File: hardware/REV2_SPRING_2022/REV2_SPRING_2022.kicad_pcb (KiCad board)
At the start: 2 copper layers, 108 x 304.8 mm, 52 parts, among them J101 Screw_Terminal_01x02, J102 Screw_Terminal_01x02, J103 Conn_01x02_Female, J104 Screw_Terminal_01x02, J105 Conn_01x02_Female, J106 Conn_01x02_Female, J107 Screw_Terminal_01x02, J108 Screw_Terminal_01x02, J109 Conn_01x02_Female, J110 Conn_01x02_Female, Q101 Q_NMOS_GDS, Q102 Q_NMOS_GDS, U1 Teensy3.6_All_Pins, U2 PA16165_Breakout, U201 TPS2113ADRBR, U3 MPL3115A2_Breakout, U301 TPS2113ADRBR, U4 BNO055_Breakout, U5 RFM69HCW_Breakout

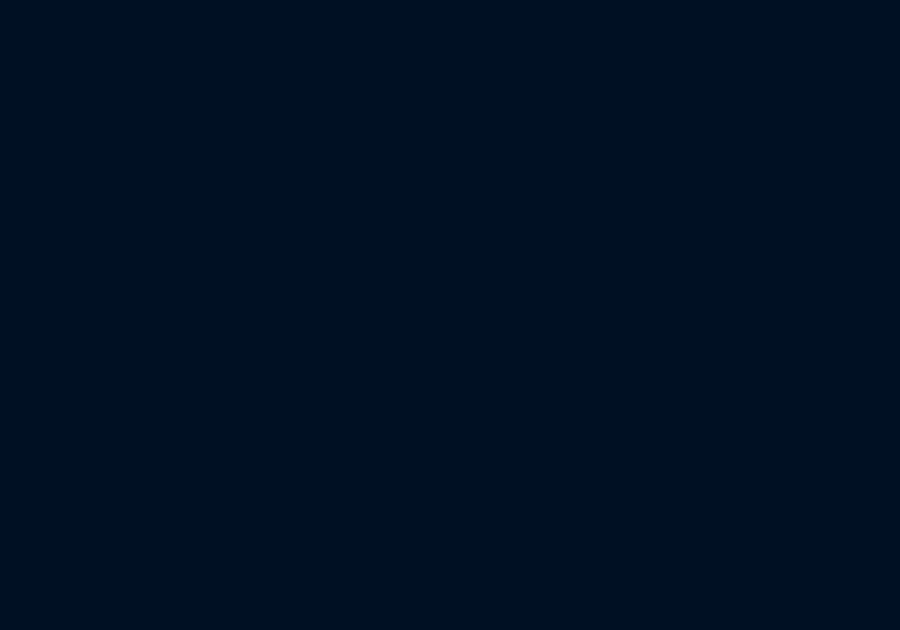
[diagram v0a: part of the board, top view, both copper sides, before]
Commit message: add another LED to schematic and layout
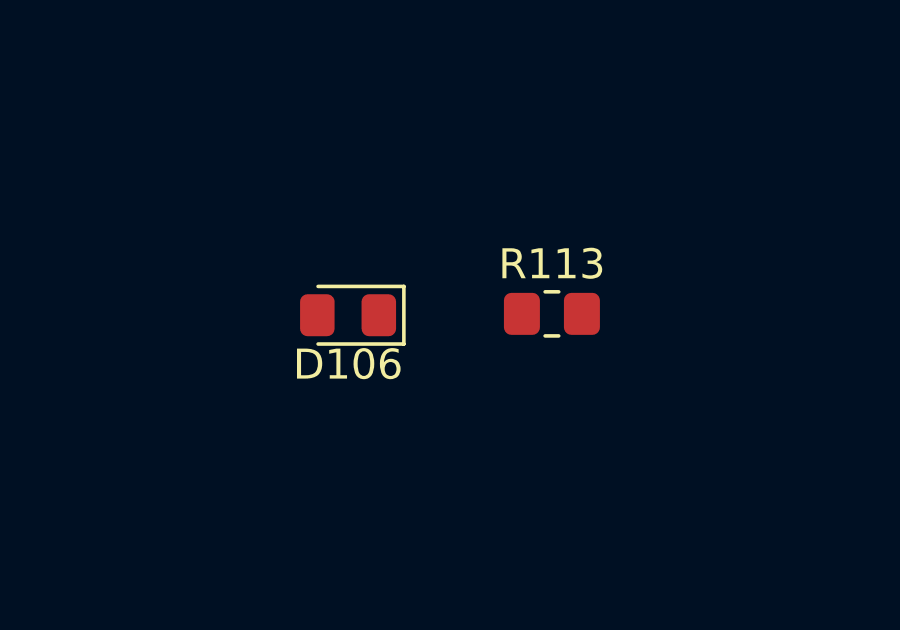
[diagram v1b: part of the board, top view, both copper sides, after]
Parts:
- added D106: LED, LED_SMD:LED_0805_2012Metric_Pad1.15x1.40mm_HandSolder, F.Cu at (197.9, 85.0)
- added R113: R_750, Resistor_SMD:R_0805_2012Metric_Pad1.20x1.40mm_HandSolder, F.Cu at (204.7, 85.0)
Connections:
- U1 pad 6: Net-(U1-Pad6) -> /BUZZER
- U1 pad 7: /BUZZER -> /LED_0

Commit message: wip
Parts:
- moved BZ101 398.2 mm to (-146.5, 21.5)
- moved R112 369.1 mm to (-97.5, -41.5), turned to 180 degrees
- moved J107 347.8 mm to (-82.8, -51.2), turned to 180 degrees
- moved R111 319.2 mm to (-46.8, -43.2), turned to 180 degrees
- moved J109 301.9 mm to (-67.8, -10.8), turned to 180 degrees
- moved J105 295.3 mm to (-82.5, -10.5), turned to 180 degrees
- moved R107 286.6 mm to (-125.5, 148.4), turned to 180 degrees
- moved R106 284.9 mm to (-125.5, 142.3), turned to 180 degrees
- moved R105 283.8 mm to (-125.5, 136.2), turned to 180 degrees
- moved R104 283.1 mm to (-125.5, 130.1), turned to 180 degrees
- moved R108 282.9 mm to (-122.4, 154.5), turned to 180 degrees
- moved J110 278.5 mm to (-33.5, -11.0), turned to 180 degrees
- moved D104 271.6 mm to (-117.9, 148.4), turned to 0 degrees
- moved D103 269.8 mm to (-117.9, 142.3), turned to 0 degrees
- moved D102 268.6 mm to (-117.9, 136.2), turned to 0 degrees
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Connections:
- net /TPS2113A for E-match/IN1 renamed /BAT1
- net /TPS2113A for E-match/IN2 renamed /BAT2
- net /TPS2113A for E-match/VOUT renamed /V_EMATCH_TO_KEY_SWITCH
- net /TPS2113A for Teensy power/VOUT renamed /VIN_TO_TEENSY_TO_KEY_SWITCH
- net Net-(J101-Pad2) renamed /EMATCH_1+
- net Net-(J102-Pad2) renamed /EMATCH_2+
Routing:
- net GND: track 1067.6 -> 354.4 mm, vias 175 -> 23
- net /V_TEENSY: track 108.0 -> 34.1 mm
- net /V_EMATCH: track 50.9 -> 7.15 mm
- net /EMATCH_1+: track 12.0 -> 0.00 mm
- net Net-(Q101-Pad1): track 9.76 -> 0.00 mm
- net /EMATCH_2+: track 9.51 -> 0.00 mm
- net /E-MATCH_TRIGGER_2: track 39.7 -> 31.3 mm
- net Net-(Q102-Pad1): track 8.36 -> 0.00 mm
- net /E-MATCH_TRIGGER_1: track 33.4 -> 28.0 mm
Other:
- outline, holes or cut-outs redrawn

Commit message: wip
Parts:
- moved Q102 50.2 mm to (-111.0, 10.6)
- moved R109 50.2 mm to (-111.0, 17.0)
- moved R112 50.2 mm to (-105.8, 8.00)
- moved Q101 46.9 mm to (-46.6, 5.67)
- moved R103 46.9 mm to (-46.5, 12.0)
- moved R111 46.9 mm to (-39.2, 3.00)
- moved J105 10.6 mm to (-93.0, -12.2)
- moved J107 10.6 mm to (-93.2, -53.0)
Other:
- board text added: "DROGUE EMATCH"
- board text added: "KEY SWITCH WIRES 1 & 2"
- board text added: "MAIN EMATCH"
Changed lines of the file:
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@@
   (general
     (thickness 1.6)
-    (drawings 21)
+    (drawings 24)
     (tracks 339)
     (zones 0)
@@
   )
   (module footprints:TO-220-3 (layer F.Cu)
-    (at -54.058 -40.582 90)
+    (at -46.558 5.668 90)
     (descr http://www.st.com/content/ccc/resource/technical/document/datasheet/f9/ed/f5/44/26/b9/43/a4/CD00000911.pdf/files/CD00000911.pdf/jcr:content/translations/en.CD00000911.pdf)
     (fp_text reference Q101 (at 2.62 -3.22 270) (layer F.SilkS)
@@
   )
   (module Resistor_SMD:R_0805_2012Metric_Pad1.20x1.40mm_HandSolder (layer F.Cu)
-    (at -54 -34.25 270)
+    (at -46.5 12 270)
     (descr "Resistor SMD 0805 (2012 Metric), square (rectangular) end terminal, IPC_7351 nominal with elongated pad for handsoldering. (Body size source: IPC-SM-782 page 72, https://www.pcb-3d.com/wordpress/wp-content/uploads/ipc-sm-782a_amendment_1_and_2.pdf), generated with kicad-footprint-generator")
     (tags "resistor handsolder")
@@
   )
   (module footprints:TO-220-3 (layer F.Cu)
-    (at -102.706 -38.89 90)
+    (at -110.956 10.61 90)
     (descr http://www.st.com/content/ccc/resource/technical/document/datasheet/f9/ed/f5/44/26/b9/43/a4/CD00000911.pdf/files/CD00000911.pdf/jcr:content/translations/en.CD00000911.pdf)
     (fp_text reference Q102 (at 2.62 -3.22 270) (layer F.SilkS)
@@
   )
   (module Resistor_SMD:R_0805_2012Metric_Pad1.20x1.40mm_HandSolder (layer F.Cu)
-    (at -102.75 -32.5 270)
+    (at -111 17 270)
     (descr "Resistor SMD 0805 (2012 Metric), square (rectangular) end terminal, IPC_7351 nominal with elongated pad for handsoldering. (Body size source: IPC-SM-782 page 72, https://www.pcb-3d.com/wordpress/wp-content/uploads/ipc-sm-782a_amendment_1_and_2.pdf), generated with kicad-footprint-generator")
     (tags "resistor handsolder")
@@
   )
   (module Connector_Wire:SolderWire-1sqmm_1x02_P5.4mm_D1.4mm_OD2.7mm_Relief2x (layer F.Cu)
-    (at -82.5 -10.5 180)
+    (at -93 -12.25 180)
     (descr "Soldered wire connection with double feed through strain relief, for 2 times 1 mm² wires, basic insulation, conductor diameter 1.4mm, outer diameter 2.7mm, size source Multi-Contact FLEXI-E 1.0 (https://ec.staubli.com/AcroFiles/Catalogues/TM_Cab-Main-11014119_(en)_hi.pdf), bend radius 3 times outer diameter, generated with kicad-footprint-generator")
     (tags "connector wire 1sqmm double-strain-relief")
@@
   )
   (module TerminalBlock:TerminalBlock_bornier-2_P5.08mm (layer F.Cu)
-    (at -82.75 -51.25 180)
+    (at -93.25 -53 180)
     (descr "simple 2-pin terminal block, pitch 5.08mm, revamped version of bornier2")
     (tags "terminal block bornier2")
@@
   )
   (module Resistor_SMD:R_0805_2012Metric_Pad1.20x1.40mm_HandSolder (layer F.Cu)
-    (at -46.75 -43.25 180)
+    (at -39.25 3 180)
     (descr "Resistor SMD 0805 (2012 Metric), square (rectangular) end terminal, IPC_7351 nominal with elongated pad for handsoldering. (Body size source: IPC-SM-782 page 72, https://www.pcb-3d.com/wordpress/wp-content/uploads/ipc-sm-782a_amendment_1_and_2.pdf), generated with kicad-footprint-generator")
     (tags "resistor handsolder")
@@
   )
   (module Resistor_SMD:R_0805_2012Metric_Pad1.20x1.40mm_HandSolder (layer F.Cu)
-    (at -97.5 -41.5 180)
+    (at -105.75 8 180)
     (descr "Resistor SMD 0805 (2012 Metric), square (rectangular) end terminal, IPC_7351 nominal with elongated pad for handsoldering. (Body size source: IPC-SM-782 page 72, https://www.pcb-3d.com/wordpress/wp-content/uploads/ipc-sm-782a_amendment_1_and_2.pdf), generated with kicad-footprint-generator")
     (tags "resistor handsolder")
@@
     )
   )
+  (gr_text "MAIN\nEMATCH" (at -37 -60.75) (layer F.SilkS)
+    (effects (font (size 1.5 1.5) (thickness 0.3)))
+  )
+  (gr_text "DROGUE\nEMATCH" (at -71 -60.25) (layer F.SilkS)
+    (effects (font (size 1.5 1.5) (thickness 0.3)))
+  )
+  (gr_text "KEY SWITCH\nWIRES 1 & 2" (at -97.25 -60.5) (layer F.SilkS)
+    (effects (font (size 1.5 1.5) (thickness 0.3)))
+  )
   (gr_line (start -13.5 -68) (end -13.500001 236.8) (layer Edge.Cuts) (width 0.2))

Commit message: wip
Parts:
- moved R110 154.7 mm to (3.00, 86.5), turned to 270 degrees
- moved J103 72.1 mm to (-34.0, -15.0), turned to 180 degrees
- moved J110 55.1 mm to (-88.5, -15.0)
- moved J102 55.1 mm to (-88.8, -56.5)
- moved J104 55.0 mm to (-34.0, -55.5), turned to 180 degrees
- moved J105 42.1 mm to (-51.0, -15.0)
- moved J107 37.4 mm to (-56.0, -56.0), turned to 0 degrees
- moved R111 35.8 mm to (-73.0, -9.00)
- moved Q101 26.2 mm to (-71.5, -2.50), turned to 180 degrees
- moved R103 26.1 mm to (-71.5, 4.50)
- moved Q102 23.5 mm to (-91.5, -2.50), turned to 180 degrees
- moved R109 23.2 mm to (-91.5, 4.50)
- moved R112 21.4 mm to (-92.8, -9.00)
- moved J109 4.43 mm to (-69.0, -15.0)
- moved J101 4.32 mm to (-68.5, -56.0)
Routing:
- net /V_EMATCH: track 7.15 -> 175.5 mm
- net /EMATCH_2+: track 0.00 -> 57.3 mm
- net /EMATCH_1+: track 0.00 -> 56.6 mm
- net /V_EMATCH_TO_KEY_SWITCH: track 0.00 -> 43.5 mm
- net /KEY_SWITCH_DIGITAL: track 0.00 -> 43.2 mm
- net /3.3V: track 215.0 -> 258.0 mm
- net Net-(Q101-Pad1): track 0.00 -> 6.02 mm
- net Net-(Q102-Pad1): track 0.00 -> 6.00 mm
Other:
- board text added: "KEY SWITCH WIRES 3 & 4"

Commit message: wip
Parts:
- moved J106 553.4 mm to (-242.0, 393.0)
- moved J108 553.4 mm to (-237.0, 381.0)
- moved R113 262.3 mm to (-51.5, 28.5), turned to 270 degrees
- moved D106 257.5 mm to (-51.5, 21.0), turned to 90 degrees
- moved D105 165.8 mm to (-21.0, 17.8), turned to 90 degrees
- moved R108 164.1 mm to (-21.0, 25.4), turned to 270 degrees
- moved D104 156.5 mm to (-27.1, 20.9), turned to 90 degrees
- moved R107 155.1 mm to (-27.1, 28.5), turned to 270 degrees
- moved D103 148.0 mm to (-33.2, 20.9), turned to 90 degrees
- moved R106 146.5 mm to (-33.2, 28.5), turned to 270 degrees
- moved D102 139.5 mm to (-39.3, 20.9), turned to 90 degrees
- moved R105 137.9 mm to (-39.3, 28.5), turned to 270 degrees
- moved D101 131.1 mm to (-45.4, 20.9), turned to 90 degrees
- moved R104 129.4 mm to (-45.4, 28.5), turned to 270 degrees
- moved C202 83.1 mm to (-80.7, 155.7), turned to 90 degrees
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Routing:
- net GND: track 354.4 -> 159.2 mm, vias 23 -> 6
- net /LED_4: track 57.4 -> 0.01 mm, vias 2 -> 0
- net /LED_3: track 56.1 -> 0.26 mm, vias 2 -> 0
- net /LED_2: track 54.4 -> 0.12 mm, vias 2 -> 0
- net /LED_1: track 53.0 -> 0.14 mm, vias 2 -> 0
- net /TPS_1_STAT: track 55.8 -> 3.80 mm, vias 1 -> 0
- net /TPS_2_STAT: track 51.1 -> 5.71 mm, vias 1 -> 0
- net /BAT2: track 82.6 -> 38.4 mm
- net /BALANCE_CONTROL: track 44.0 -> 0.00 mm, vias 1 -> 0
- net /3.3V: track 258.0 -> 218.4 mm
- net /V_TEENSY: track 34.1 -> 3.35 mm, vias 2 -> 0
- net /E-MATCH_TRIGGER_1: track 28.0 -> 0.00 mm, vias 1 -> 0
- net /TPS2113A for E-match/VSNS: track 7.49 -> 29.9 mm, vias 0 -> 2
- net /BAT1: track 69.5 -> 48.5 mm
- net /V_EMATCH_TO_KEY_SWITCH: track 43.5 -> 62.0 mm
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
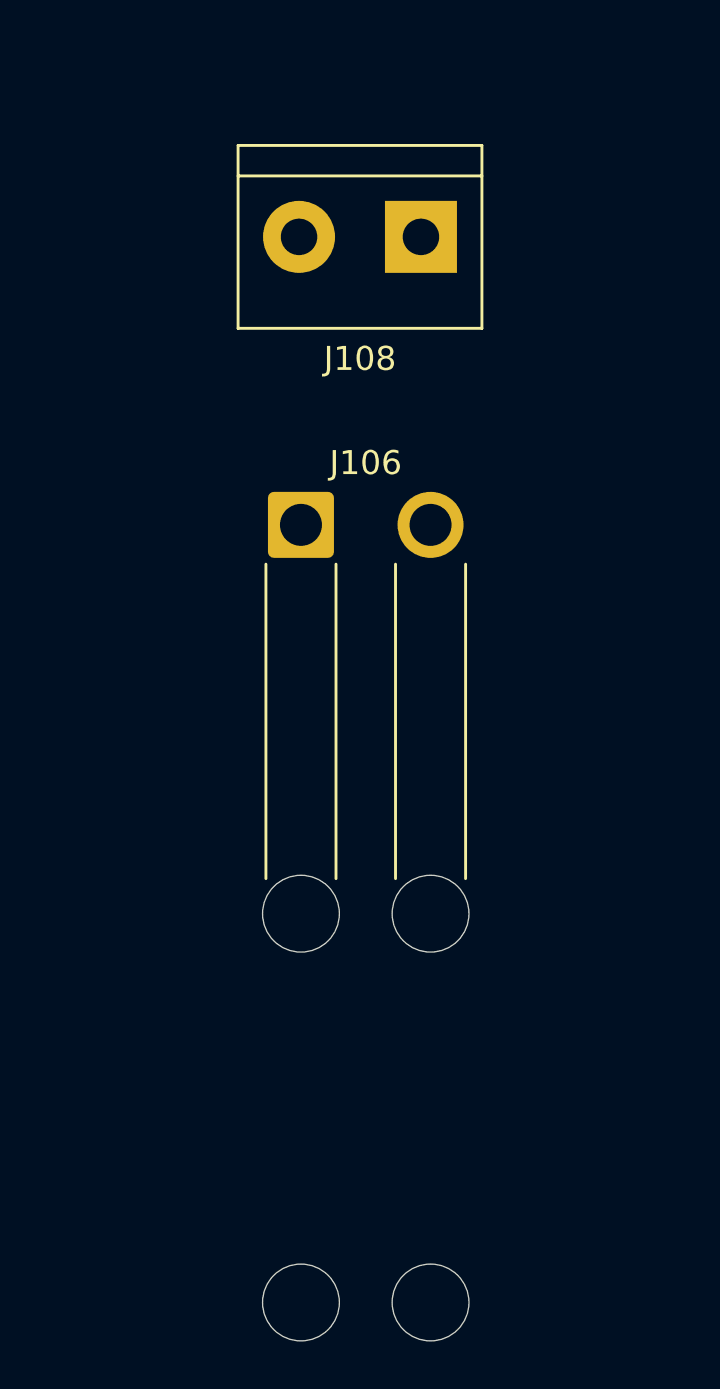
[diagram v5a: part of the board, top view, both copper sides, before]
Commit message: remove hardware electrical arming (now using software arming)
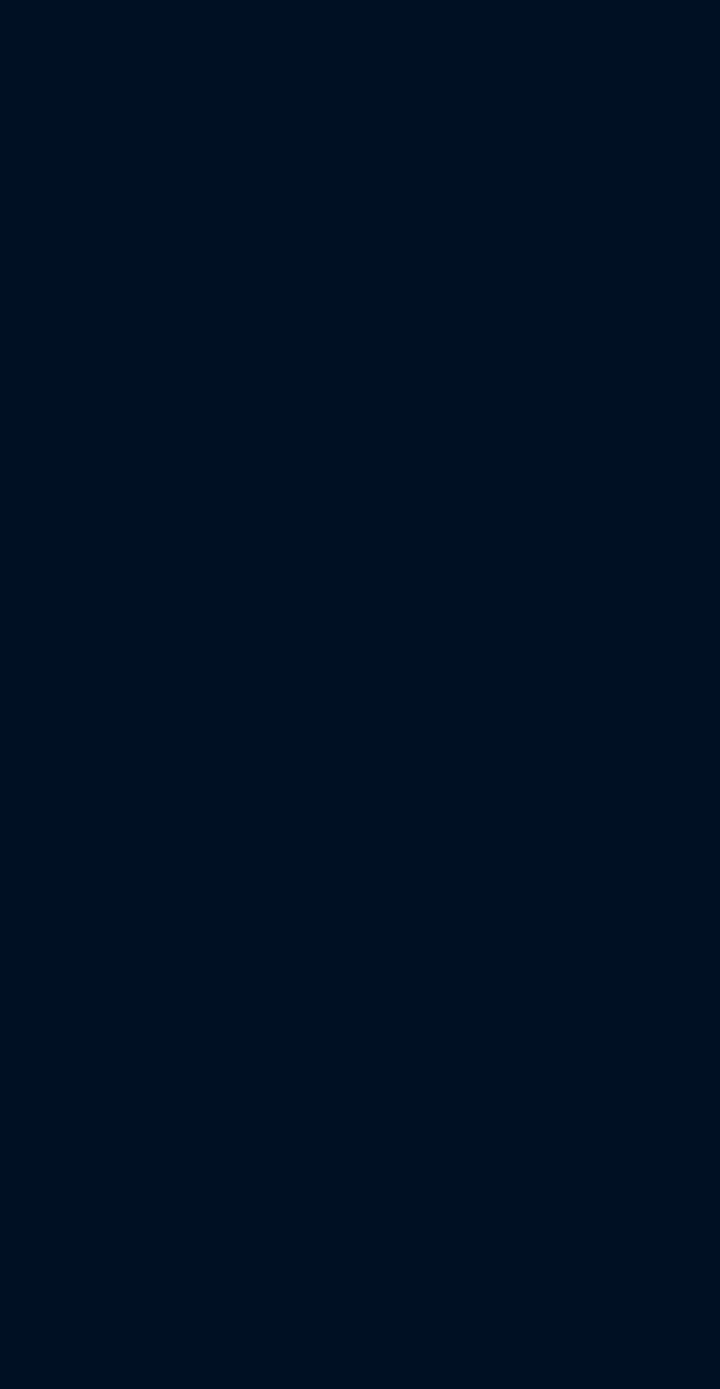
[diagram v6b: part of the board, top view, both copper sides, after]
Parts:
- removed J106: Conn_01x02_Female, Connector_Wire:SolderWire-1sqmm_1x02_P5.4mm_D1.4mm_OD2.7mm_Relief2x
- removed J108: Screw_Terminal_01x02, TerminalBlock:TerminalBlock_bornier-2_P5.08mm
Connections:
- C303 pad 1: /VIN_TO_TEENSY_TO_KEY_SWITCH -> /V_TEENSY
- R302 pad 1: /VIN_TO_TEENSY_TO_KEY_SWITCH -> /V_TEENSY
- U301 pad 7: /VIN_TO_TEENSY_TO_KEY_SWITCH -> /V_TEENSY
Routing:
- net /VIN_TO_TEENSY_TO_KEY_SWITCH: track 8.49 -> 0.00 mm
- net /V_TEENSY: track 3.35 -> 11.8 mm

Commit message: wip
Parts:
- moved C101 25.3 mm to (-51.4, 87.3)
- moved U1 25.3 mm to (-60.1, 119.9)
- moved U2 25.3 mm to (-89.3, 102.1)
- moved U3 25.3 mm to (-39.8, 98.3)
- moved U4 25.3 mm to (-36.0, 127.0)
- moved U5 25.3 mm to (-87.3, 137.6)
- moved C201 8.40 mm to (-74.0, 170.6)
- moved C202 8.40 mm to (-73.0, 158.9)
- moved C203 8.40 mm to (-74.0, 165.8)
- moved C301 8.40 mm to (-53.3, 170.7)
- moved C302 8.40 mm to (-53.3, 159.3)
- moved C303 8.40 mm to (-54.1, 165.7)
- moved R101 8.40 mm to (-41.4, 167.1)
- moved R102 8.40 mm to (-37.9, 167.2)
- moved R201 8.40 mm to (-66.3, 158.9)
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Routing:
- net /V_EMATCH_TO_KEY_SWITCH: track 62.0 -> 50.5 mm
- net /V_TEENSY: track 11.8 -> 17.9 mm

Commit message: wip
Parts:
- BZ101: moved to B.Cu
- moved BZ101 268.5 mm to (83.2, 160.5), turned to 180 degrees
- moved U2 231.2 mm to (139.1, 137.4), turned to 270 degrees
- moved U5 227.2 mm to (137.1, 101.9), turned to 180 degrees
- moved R201 182.8 mm to (116.5, 161.7)
- moved BT101 181.5 mm to (150.6, 188.7)
- moved BT102 181.5 mm to (150.6, 210.3)
- moved C201 181.5 mm to (107.5, 173.4)
- moved C202 181.5 mm to (108.5, 161.7)
- moved C203 181.5 mm to (107.5, 168.5)
- moved C301 181.5 mm to (128.2, 173.5)
- moved C302 181.5 mm to (128.2, 162.0)
- moved C303 181.5 mm to (127.4, 168.4)
- moved D101 181.5 mm to (136.1, 23.6)
- moved D102 181.5 mm to (142.2, 23.6)
- moved D103 181.5 mm to (148.3, 23.6)
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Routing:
- net /V_EMATCH_TO_KEY_SWITCH: track 50.5 -> 298.5 mm
- net /BUZZER: track 0.00 -> 41.8 mm
- net /E-MATCH_TRIGGER_2: track 31.3 -> 0.00 mm, vias 1 -> 0
- net /V_TEENSY: track 17.9 -> 45.7 mm
- net /SCK: track 69.6 -> 65.6 mm, vias 6 -> 2
- net GND: track 159.2 -> 156.1 mm, vias 6 -> 5
- net Net-(R201-Pad2): track 4.60 -> 4.08 mm
